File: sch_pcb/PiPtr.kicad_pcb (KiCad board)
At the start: 4 copper layers, 101.6 x 141.7 mm, 348 parts, among them J101 GLOBAL_LINK_LEFT, J102 GLOBAL_LINK_RIGHT, J103 RTC, J107 RASPBERRY_PI, J111 FP_PIXEL, J112 AM2302, J113 I2C1_5V, J204 DE9F, J301 SPARE, J302 SPARE, J303 SPARE, J304 SPARE, J305 AUX_IO_1, J306 SPARE, J307 SPARE, J308 AUX_IO_2, J309 SPARE, J310 SPARE, J313 SPARE, J314 SPARE, J404 DE9F, J501 MicroUSB, P301 Chassis, Q101 BSS138, Q102 BSS138, Q103 BSS138, Q104 BSS138, Q105 BSS138, Q201 BSS138, Q202 BSS138, Q203 BSS138, Q301 SPARE, Q302 SPARE, Q401 BSS138, Q402 BSS138, Q403 BSS138, U101 MCP23017, U102 IP4234CZ6, U103 MCP4351, U104 74HCT138, U105 74LV1T125, U107 MCP4351, U108 IP4234CZ6, U110 74LV1T125, U111 74LV1T125, U112 74LV1T125, U113 74LV1T125, U201 MCP6004N, U202 74LVC1G3157, U203 74LVC1G3157, U204 74LVC4066, U205 MCP6004N, U206 74LVC1G3157, U207 MCP6S26, U301 MCP23017, U302 SPARE, U303 SPARE, U304 MCP3008, U305 MCP1703A-2502/MB, U306 TPS54302, U307 IP4234CZ6, U401 MCP6004N, U402 74LVC1G3157, U403 74LVC1G3157, U404 74LVC4066, U405 MCP6004N, U406 74LVC1G3157, U407 MCP6S26, U501 CM108B, U502 CM108B, U503 TUSB2036, Y501 6MHz

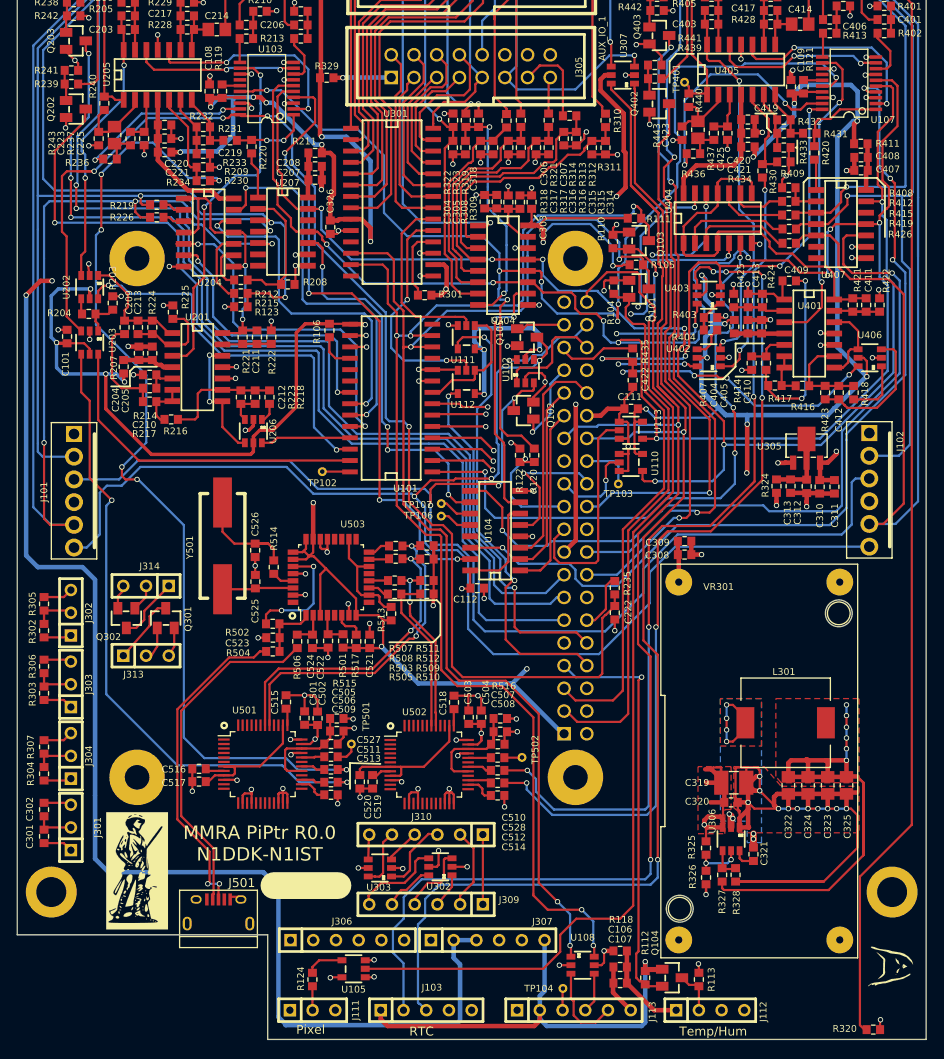
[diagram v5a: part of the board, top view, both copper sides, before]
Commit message: Add files via upload
Add a PMOS switch to allow turning on the soundcard section (hub and 2 soundcard chips) after the Pi has booted.  For some reason, doing so before the desktop loads causes it to hang..
Change gain resistors in opamp stages to move the sweet spot closer to the center of the digital pots to allow for more adjustment range
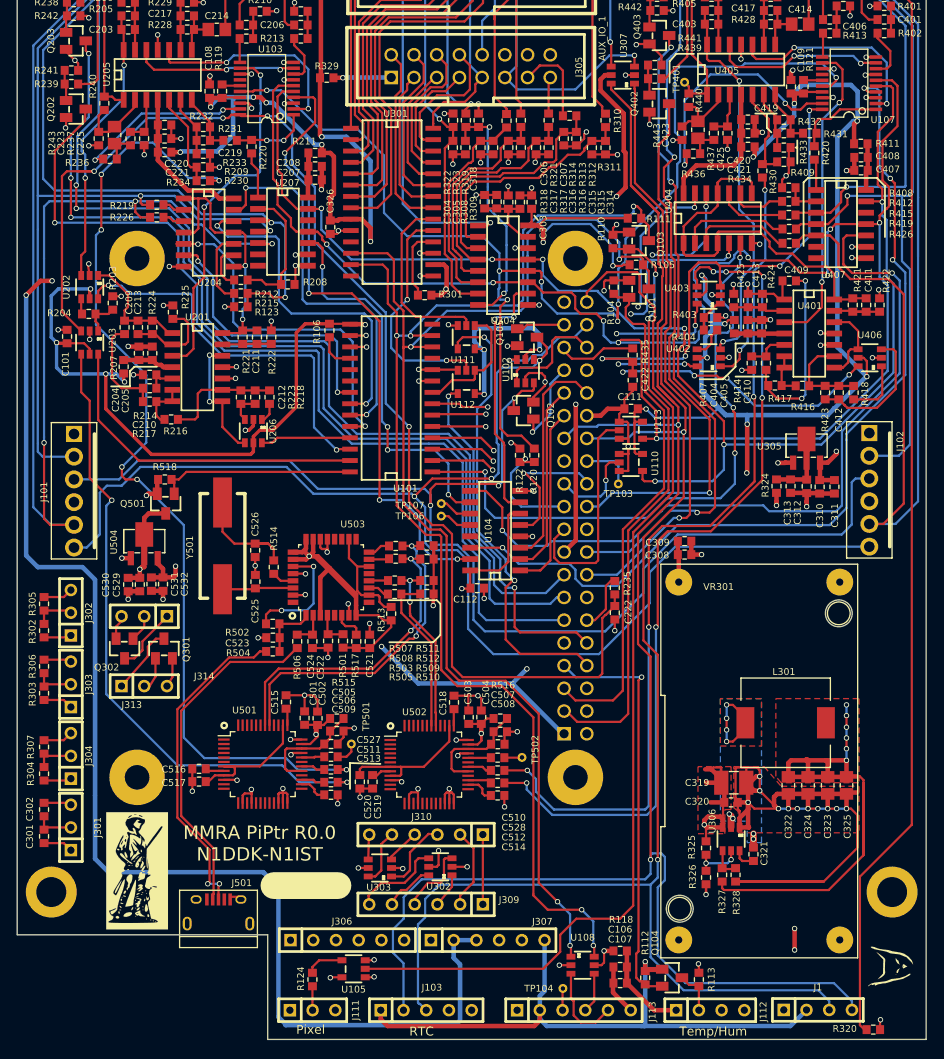
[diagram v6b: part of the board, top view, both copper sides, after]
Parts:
- removed TP102: TESTPOINT, lib:Wire_28AWG
- added C529: 4.7u, lib:smd0603, F.Cu at (70.8, 118.8)
- added C530: 0.1u, lib:smd0603, F.Cu at (69.5, 118.8)
- added C531: 0.1u, lib:smd0603, F.Cu at (72.2, 118.7)
- added C532: 4.7u, lib:smd0603, F.Cu at (73.5, 118.7)
- added J1: OLED_SSD1306, lib:SIL-4, F.Cu at (146.7, 166.3)
- added Q501: BSR315PH6327XTSA1, lib:SOT23, F.Cu at (73.8, 109.7)
- added R518: 10k, lib:smd0603, F.Cu at (73.7, 107.0)
- added U504: MCP1703A-3302/MB, lib:sot89, F.Cu at (71.3, 113.9)
- R205, R224, R228, R232, R405, R424, R428, R432: value 10k -> 100k
- moved J314 3.41 mm to (71.3, 122.3)
- moved J313 3.41 mm to (71.3, 130.1)
- moved Q301 3.41 mm to (73.5, 125.9)
- moved Q302 3.41 mm to (69.2, 125.9)
- turned R515 to 0 degrees
- turned R516 to 0 degrees
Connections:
- C501 pad 1: +5V -> +5VP
- C502 pad 1: +5V -> +5VP
- C503 pad 1: +5V -> +5VP
- C504 pad 1: +5V -> +5VP
- C521 pad 2: +3V3 -> +3.3VP
- R501 pad 2: +3V3 -> +3.3VP
- R513 pad 2: +3V3 -> +3.3VP
- R515 pad 2: +5V -> +5VP
- R516 pad 2: +5V -> +5VP
- R517 pad 2: +3V3 -> +3.3VP
- U101 pad 28: Net-(TP102-Pad1) -> /soundcard/SOUNDCARD_EN
- U501 pad 35: +5V -> +5VP
- U502 pad 35: +5V -> +5VP
- U503 pad 23: +3V3 -> +3.3VP
- U503 pad 24: +3V3 -> +3.3VP
- U503 pad 25: +3V3 -> +3.3VP
- U503 pad 26: +3V3 -> +3.3VP
- U503 pad 3: +3V3 -> +3.3VP
- U503 pad 8: +3V3 -> +3.3VP
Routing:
- net +5VP: track 0.00 -> 73.1 mm, vias 0 -> 3
- net +3.3VP: track 0.00 -> 65.9 mm, vias 0 -> 2
- net /SDA0_33: track 157.0 -> 195.5 mm
- net /SCL0_33: track 149.9 -> 181.0 mm
- net +3V3: track 672.8 -> 647.5 mm, vias 13 -> 12
- net /soundcard/SOUNDCARD_EN: track 0.00 -> 22.1 mm
- net +5V: track 457.8 -> 447.1 mm, vias 44 -> 41
- net GND: track 343.1 -> 348.6 mm, vias 119 -> 122
- net Net-(TP102-Pad1): track 3.11 -> 0.00 mm
- net (no net): track 0.00 -> 2.40 mm, vias 0 -> 2
- net /CH1/TONE_FROM_PI: track 145.7 -> 144.8 mm
- net /PTT1D: track 121.8 -> 121.0 mm
- net /LINK2_AUD: track 367.5 -> 366.8 mm
- net /LINK1_AUD: track 280.7 -> 280.0 mm
- net /CH1/LOCAL_LINK: track 221.9 -> 221.2 mm
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
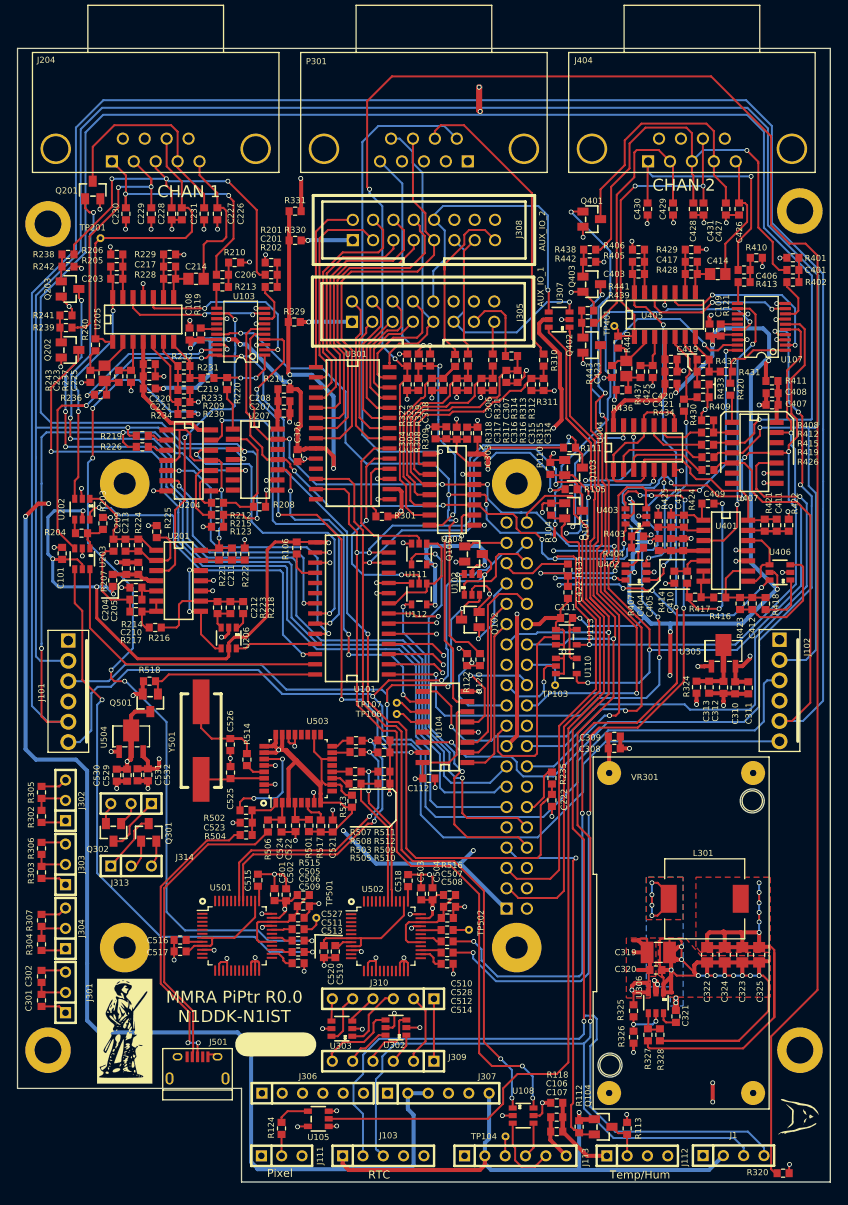
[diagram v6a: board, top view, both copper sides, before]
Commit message: Update board with third soundcard
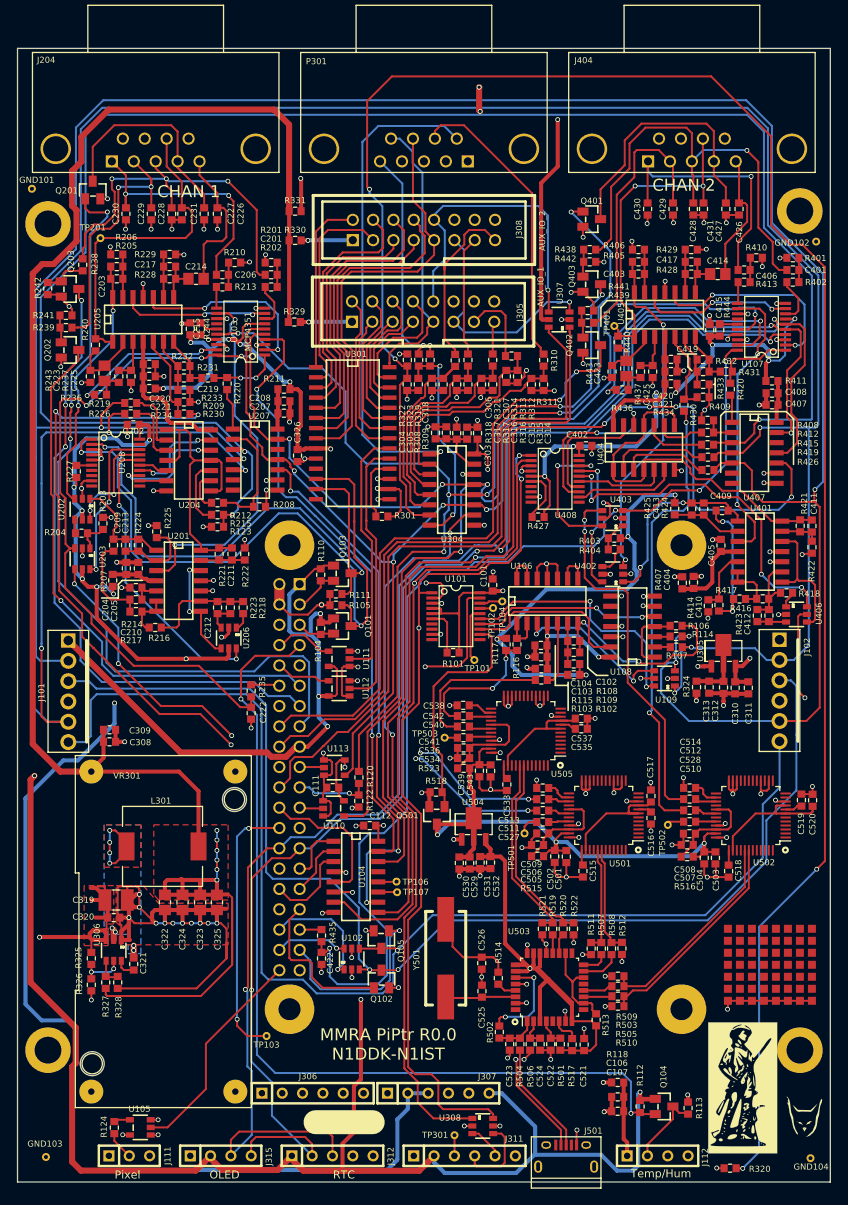
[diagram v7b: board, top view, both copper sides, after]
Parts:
- removed C108, C109: 0.1u, lib:smd0603
- removed C301, C302, R302, R303, R304, R305, R306, R307: SPARE, lib:smd0603
- removed G***: LOGO, lib:mmra_logo1
- removed J1: OLED_SSD1306, lib:SIL-4
- removed J103: RTC, lib:SIL-5
- removed J113: I2C1_5V, lib:SIL-6
- removed J301, J302, J303, J304, J313, J314: SPARE, lib:SIL-3
- removed J309, J310: SPARE, lib:SIL-6
- removed Q301, Q302: SPARE, lib:SOT23
- removed R119, R121: 10k, lib:smd0603
- removed U302, U303: SPARE, lib:SOT23-6
- added C102: 33p, lib:smd0603, F.Cu at (126.7, 102.0)
- added C103: 4.7u, lib:smd0603, F.Cu at (122.6, 104.0)
- added C104: 0.1u, lib:smd0603, F.Cu at (122.6, 102.6)
- added C202: 0.1u, lib:smd0603, F.Cu at (71.6, 75.0)
- added C215: 0.1u, lib:smd0603, F.Cu at (78.8, 63.0)
- added C402: 0.1u, lib:smd0603, F.Cu at (128.2, 77.6)
- added C415: 0.1u, lib:smd0603, F.Cu at (143.7, 63.2)
- added C533: 4u7, lib:smd0603, F.Cu at (118.3, 120.0)
- added C534: 4u7, lib:smd0603, F.Cu at (112.9, 116.7)
- added C535: 4u7, lib:smd0603, F.Cu at (127.6, 113.0)
- added C536: 100n, lib:smd0603, F.Cu at (112.9, 115.4)
- added C537: 4u7, lib:smd0603, F.Cu at (127.6, 111.7)
- added C538: 4u7, lib:smd0603, F.Cu at (112.9, 110.1)
- added C539: 4u7, lib:smd0603, F.Cu at (114.9, 118.2)
- added C540: 10u, lib:smd0603, F.Cu at (112.9, 112.7)
- added C541: 10u, lib:smd0603, F.Cu at (112.9, 114.1)
- added C542: 10u, lib:smd0603, F.Cu at (112.9, 111.4)
- added C543: 100n, lib:smd0603, F.Cu at (116.3, 118.3)
- added GND101: TESTPOINT, lib:Wire_28AWG, F.Cu at (59.0, 45.5)
- added GND102: TESTPOINT, lib:Wire_28AWG, F.Cu at (157.0, 52.1)
- added GND103: TESTPOINT, lib:Wire_28AWG, F.Cu at (60.7, 166.5)
- added GND104: TESTPOINT, lib:Wire_28AWG, F.Cu at (156.3, 166.7)
- added J311: I2C1_5V, lib:SIL-6, F.Cu at (113.0, 166.4)
- added J312: RTC, lib:SIL-5, F.Cu at (97.8, 166.4)
- added J315: OLED_SSD1306, lib:SIL-4, F.Cu at (82.5, 166.4)
- added LOGO302: MOUNTING_HOLE, lib:mmra_logo, F.Cu at (147.8, 157.8)
- added PROTO301: MOUNTING_HOLE, lib:SMD_proto_area, F.Cu at (151.2, 142.5)
- added R101: 10k, lib:smd0603, F.Cu at (111.6, 103.5)
- added R102: 10k, lib:smd0603, F.Cu at (126.7, 106.2)
- added R103: 1k, lib:smd0603, F.Cu at (122.6, 106.9)
- added R107: 2k, lib:smd0603, F.Cu at (139.5, 102.8)
- added R108: 100k, lib:smd0603, F.Cu at (126.7, 103.4)
- added R109: 10k, lib:smd0603, F.Cu at (126.7, 104.9)
- added R114: 2k, lib:smd0603, F.Cu at (139.5, 101.4)
- added R115: 33, lib:smd0603, F.Cu at (122.6, 105.5)
- added R116: 3k3, lib:smd0603, F.Cu at (119.6, 102.4)
- added R117: 1k, lib:smd0603, F.Cu at (118.2, 102.4)
- added R227: 10k, lib:smd0603, F.Cu at (64.5, 80.8)
- added R244: 10k, lib:smd0603, F.Cu at (80.0, 63.0)
- added R427: 10k, lib:smd0603, F.Cu at (122.2, 86.5)
- added R444: 10k, lib:smd0603, F.Cu at (144.9, 63.1)
- added R519: 22R, lib:smd0603, F.Cu at (124.0, 138.0)
- added R520: 22R, lib:smd0603, F.Cu at (125.3, 138.0)
- added R521: 15k, lib:smd0603, F.Cu at (122.8, 138.0)
- added R522: 15k, lib:smd0603, F.Cu at (126.7, 138.0)
- added R523: 33R, lib:smd0603, F.Cu at (112.9, 117.9)
- added TP101: TESTPOINT, lib:Wire_28AWG, F.Cu at (114.2, 104.4)
- added TP102: TESTPOINT, lib:Wire_28AWG, F.Cu at (116.6, 97.9)
- added TP301: TESTPOINT, lib:Wire_28AWG, F.Cu at (111.8, 163.8)
- added TP503: CH3_RIGHT, lib:Wire_28AWG, F.Cu at (110.5, 114.1)
- added U106: MCP6004T, lib:SOIC14, F.Cu at (123.4, 97.0)
- added U109: 74LVC1G3157, lib:SOT23-6, F.Cu at (138.0, 106.7)
- added U208: MCP23008, lib:SSOP-20, F.Cu at (69.4, 79.7)
- added U308: IP4234CZ6, lib:SOT23-6, F.Cu at (115.3, 162.6)
- added U408: MCP23008, lib:SSOP-20, F.Cu at (124.3, 81.7)
- added U505: CM108B, lib:LQFP-48_7x7mm_Pitch0.5mm, F.Cu at (120.7, 113.2)
- R106: value 10k -> 20k
- U101: value MCP23017 -> MCP23008; footprint lib:SOIC28 -> lib:SSOP-20
- U108: value IP4234CZ6 -> 74LVC4066; footprint lib:SOT23-6 -> lib:SOIC14
- U201, U205, U401, U405: value MCP6004N -> MCP6004T
- moved C319 68.1 mm to (69.5, 134.4)
- moved C323 68.1 mm to (80.0, 134.7)
- moved C324 68.1 mm to (77.8, 134.7)
- moved L301 68.1 mm to (75.3, 127.7)
- moved R325 68.1 mm to (66.4, 141.7)
- moved R326 68.1 mm to (66.4, 145.0)
- moved C320 68.1 mm to (69.2, 136.6)
- moved C321 68.1 mm to (71.7, 142.4)
- moved C322 68.1 mm to (75.6, 134.7)
- moved C325 68.1 mm to (82.1, 134.7)
- moved R327 68.1 mm to (68.2, 144.7)
- moved R328 68.1 mm to (69.7, 144.7)
- moved U306 68.1 mm to (69.2, 140.7)
- moved TP104 66.9 mm to (117.8, 97.1)
- moved VR301 64.7 mm to (75.4, 138.3)
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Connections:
- net /CH1/FROM_SOUNDCARD renamed /soundcard/FROM_SND1
- net /CH1/LOCAL_LINK renamed LOCAL_LINK_AUD
- net /CH1/TO_SOUNDCARD renamed /soundcard/TO_SND1
- net /CH2/FROM_SOUNDCARD renamed /soundcard/FROM_SND2
- net /CH2/TO_SOUNDCARD renamed /soundcard/TO_SND2
- net /LINK1_AUD renamed LINK1_AUD
- net /LINK2_AUD renamed LINK2_AUD
- J112 pad 3: (no net) -> Net-(J112-Pad3)
- J305 pad 16: (no net) -> Net-(J305-Pad16)
- J307 pad 1: (no net) -> Net-(J307-Pad1)
- J308 pad 16: (no net) -> Net-(J308-Pad16)
- J501 pad 1: (no net) -> Net-(J501-Pad1)
- J501 pad 4: (no net) -> Net-(J501-Pad4)
- MTG301 pad 1: (no net) -> Net-(MTG301-Pad1)
- MTG302 pad 1: (no net) -> Net-(MTG302-Pad1)
- MTG303 pad 1: (no net) -> Net-(MTG303-Pad1)
- MTG304 pad 1: (no net) -> Net-(MTG304-Pad1)
- Q101 pad 3: /SCL1_5 -> SCL1_5
- Q103 pad 3: /SDA1_5 -> SDA1_5
- Q501 pad 1: /soundcard/SOUNDCARD_EN -> /SC_ENA
- R105 pad 2: /SCL1_5 -> SCL1_5
- R106 pad 2: +5V -> Net-(C102-Pad1)
- R111 pad 2: /SDA1_5 -> SDA1_5
- R513 pad 1: Net-(R513-Pad1) -> +3.3VP
- R513 pad 2: +3.3VP -> Net-(R513-Pad2)
- R518 pad 1: /soundcard/SOUNDCARD_EN -> /SC_ENA
- TP104 pad 1: Net-(J113-Pad3) -> Net-(TP104-Pad1)
- U101 pad 1: /RX2_LOCAL_EN -> SCL1_5
- U101 pad 10: GND -> (no net)
- U101 pad 12: /SCL1_5 -> /SC_ENA
- U101 pad 13: /SDA1_5 -> /SC3_LINK1
- U101 pad 14: (no net) -> /SC3_LINK2
- U101 pad 15: +5V -> /SC3_LINK_SEL
- U101 pad 16: GND -> Net-(TP101-Pad1)
- U101 pad 17: GND -> Net-(TP102-Pad1)
- U101 pad 18: Net-(R106-Pad1) -> Net-(TP104-Pad1)
- U101 pad 19: (no net) -> /~UINT_ENA
- U101 pad 2: /RX2_BUS1_EN -> SDA1_5
- U101 pad 20: (no net) -> +5V
- U101 pad 3: /RX2_BUS2_EN -> GND
- U101 pad 4: /RX2_BUS3_EN -> +5V
- U101 pad 5: /RX2_DEEMP_EN -> +5V
- U101 pad 6: /RX2_DESC_EN -> Net-(R101-Pad1)
- U101 pad 7: /PORT2_DET_EN -> (no net)
- U101 pad 8: /~UINT_ENA -> (no net)
- U101 pad 9: +5V -> GND
- U103 pad 17: +5V -> GND
- U103 pad 7: GND -> +5V
- U104 pad 13: (no net) -> Net-(U104-Pad13)
- U107 pad 17: +5V -> GND
- U107 pad 7: GND -> +5V
- U108 pad 1: /SCL1_5 -> Net-(R106-Pad1)
- U108 pad 2: GND -> Net-(R107-Pad2)
- U108 pad 4: Net-(J113-Pad4) -> Net-(R106-Pad1)
- U108 pad 5: +5V -> /SC3_LINK2
- U108 pad 6: /SDA1_5 -> GND
- U202 pad 6: /RX1_DESC_EN -> /CH1/RX_DESC_EN
- U203 pad 6: /PORT1_DET_EN -> /CH1/PORT_DET_EN
- U204 pad 12: /RX1_BUS1_EN -> /CH1/RX_BUS1_EN
- U204 pad 13: /RX1_BUS2_EN -> /CH1/RX_BUS2_EN
- U204 pad 5: /RX1_BUS3_EN -> /CH1/RX_BUS3_EN
- U204 pad 6: /RX1_LOCAL_EN -> /CH1/RX_LOCAL_EN
- U206 pad 6: /RX1_DEEMP_EN -> /CH1/RX_DEEMP_EN
- U207 pad 12: (no net) -> Net-(U207-Pad12)
- U207 pad 6: (no net) -> Net-(U207-Pad6)
- U207 pad 7: (no net) -> Net-(U207-Pad7)
- U301 pad 12: /SCL1_5 -> SCL1_5
- U301 pad 13: /SDA1_5 -> SDA1_5
- U402 pad 6: /RX2_DESC_EN -> /CH2/RX_DESC_EN
- U403 pad 6: /PORT2_DET_EN -> /CH2/PORT_DET_EN
- U404 pad 12: /RX2_BUS1_EN -> /CH2/RX_BUS1_EN
- U404 pad 13: /RX2_BUS2_EN -> /CH2/RX_BUS2_EN
- U404 pad 5: /RX2_BUS3_EN -> /CH2/RX_BUS3_EN
- U404 pad 6: /RX2_LOCAL_EN -> /CH2/RX_LOCAL_EN
- U406 pad 6: /RX2_DEEMP_EN -> /CH2/RX_DEEMP_EN
- U407 pad 12: (no net) -> Net-(U407-Pad12)
- U407 pad 6: (no net) -> Net-(U407-Pad6)
- U407 pad 7: (no net) -> Net-(U407-Pad7)
- U501 pad 1: (no net) -> Net-(U501-Pad1)
- U501 pad 11: (no net) -> Net-(U501-Pad11)
- U501 pad 12: (no net) -> Net-(U501-Pad12)
- U501 pad 13: (no net) -> Net-(U501-Pad13)
- U501 pad 15: (no net) -> Net-(U501-Pad15)
- U501 pad 17: (no net) -> Net-(U501-Pad17)
- U501 pad 18: (no net) -> Net-(U501-Pad18)
- U501 pad 19: (no net) -> Net-(U501-Pad19)
- U501 pad 2: (no net) -> Net-(U501-Pad2)
- U501 pad 20: (no net) -> Net-(U501-Pad20)
- U501 pad 21: (no net) -> Net-(U501-Pad21)
- U501 pad 25: (no net) -> Net-(U501-Pad25)
- U501 pad 28: (no net) -> Net-(U501-Pad28)
- U501 pad 3: (no net) -> Net-(U501-Pad3)
- U501 pad 31: (no net) -> Net-(U501-Pad31)
- U501 pad 39: (no net) -> Net-(U501-Pad39)
- U501 pad 4: (no net) -> Net-(U501-Pad4)
- U501 pad 40: (no net) -> Net-(U501-Pad40)
- U501 pad 43: (no net) -> Net-(U501-Pad43)
- U501 pad 44: (no net) -> Net-(U501-Pad44)
- U501 pad 45: (no net) -> Net-(U501-Pad45)
- U501 pad 46: (no net) -> Net-(U501-Pad46)
- U501 pad 47: (no net) -> Net-(U501-Pad47)
- U501 pad 48: (no net) -> Net-(U501-Pad48)
- U501 pad 5: (no net) -> Net-(U501-Pad5)
- U501 pad 6: (no net) -> Net-(U501-Pad6)
- U502 pad 1: (no net) -> Net-(U502-Pad1)
- U502 pad 11: (no net) -> Net-(U502-Pad11)
- U502 pad 12: (no net) -> Net-(U502-Pad12)
- U502 pad 13: (no net) -> Net-(U502-Pad13)
- U502 pad 15: (no net) -> Net-(U502-Pad15)
- U502 pad 17: (no net) -> Net-(U502-Pad17)
- U502 pad 18: (no net) -> Net-(U502-Pad18)
- U502 pad 19: (no net) -> Net-(U502-Pad19)
- U502 pad 2: (no net) -> Net-(U502-Pad2)
- U502 pad 20: (no net) -> Net-(U502-Pad20)
- U502 pad 21: (no net) -> Net-(U502-Pad21)
- U502 pad 25: (no net) -> Net-(U502-Pad25)
- U502 pad 28: (no net) -> Net-(U502-Pad28)
- U502 pad 3: (no net) -> Net-(U502-Pad3)
- U502 pad 31: (no net) -> Net-(U502-Pad31)
- U502 pad 39: (no net) -> Net-(U502-Pad39)
- U502 pad 4: (no net) -> Net-(U502-Pad4)
- U502 pad 40: (no net) -> Net-(U502-Pad40)
- U502 pad 43: (no net) -> Net-(U502-Pad43)
- U502 pad 44: (no net) -> Net-(U502-Pad44)
- U502 pad 45: (no net) -> Net-(U502-Pad45)
- U502 pad 46: (no net) -> Net-(U502-Pad46)
- U502 pad 47: (no net) -> Net-(U502-Pad47)
- U502 pad 48: (no net) -> Net-(U502-Pad48)
- U502 pad 5: (no net) -> Net-(U502-Pad5)
- U502 pad 6: (no net) -> Net-(U502-Pad6)
- U503 pad 10: Net-(R513-Pad1) -> Net-(R513-Pad2)
- U503 pad 13: (no net) -> Net-(U503-Pad13)
- U503 pad 14: Net-(R513-Pad1) -> Net-(R513-Pad2)
- U503 pad 17: (no net) -> Net-(U503-Pad17)
- U503 pad 18: Net-(R513-Pad1) -> Net-(R513-Pad2)
- U503 pad 19: (no net) -> Net-(R520-Pad2)
- U503 pad 20: (no net) -> Net-(R519-Pad2)
- U503 pad 22: GND -> +3.3VP
- U503 pad 24: +3.3VP -> GND
- U503 pad 32: (no net) -> Net-(U503-Pad32)
- U503 pad 5: (no net) -> Net-(U503-Pad5)
- U503 pad 9: (no net) -> Net-(U503-Pad9)
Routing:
- net SCL1_5: track 0.00 -> 205.3 mm, vias 0 -> 5
- net SDA1_5: track 0.00 -> 187.3 mm, vias 0 -> 4
- net /SCL1_5: track 142.2 -> 0.00 mm, vias 4 -> 0
- net /SDA1_5: track 141.8 -> 0.00 mm, vias 5 -> 0
- net +3V3: track 647.5 -> 541.3 mm, vias 12 -> 10
- net /PIXEL_33: track 116.1 -> 27.8 mm
- net +5V: track 447.1 -> 534.7 mm, vias 41 -> 46
- net /CH2/TONE_FROM_PI: track 57.8 -> 129.7 mm
- net /RX2_BUS1_EN: track 71.5 -> 0.00 mm, vias 3 -> 0
- net /RX2_LOCAL_EN: track 70.5 -> 0.00 mm, vias 4 -> 0
- net /RX2_BUS2_EN: track 67.2 -> 0.00 mm, vias 3 -> 0
- net /DHT_33: track 46.3 -> 113.4 mm, vias 1 -> 2
- net /RX2_BUS3_EN: track 63.0 -> 0.00 mm, vias 3 -> 0
- net /RX2_DEEMP_EN: track 62.5 -> 0.00 mm, vias 5 -> 0
- net /CH1/TONE_FROM_PI: track 144.8 -> 83.4 mm, vias 4 -> 3
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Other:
- outline, holes or cut-outs redrawn
- board text added: "OLED"
